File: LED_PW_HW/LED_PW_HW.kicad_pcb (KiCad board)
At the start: 2 copper layers, 44 x 44 mm, 0 parts

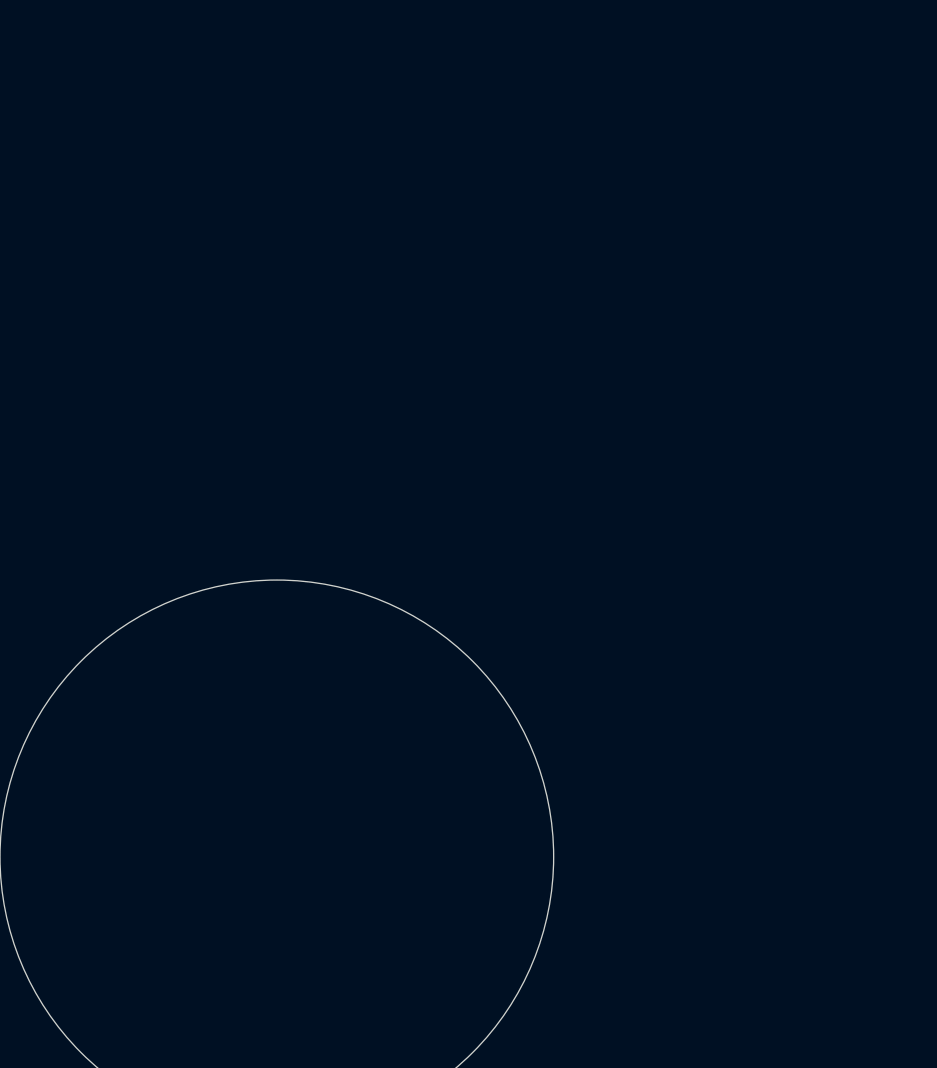
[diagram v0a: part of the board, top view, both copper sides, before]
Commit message: imported first footprints to pcb to get an idea
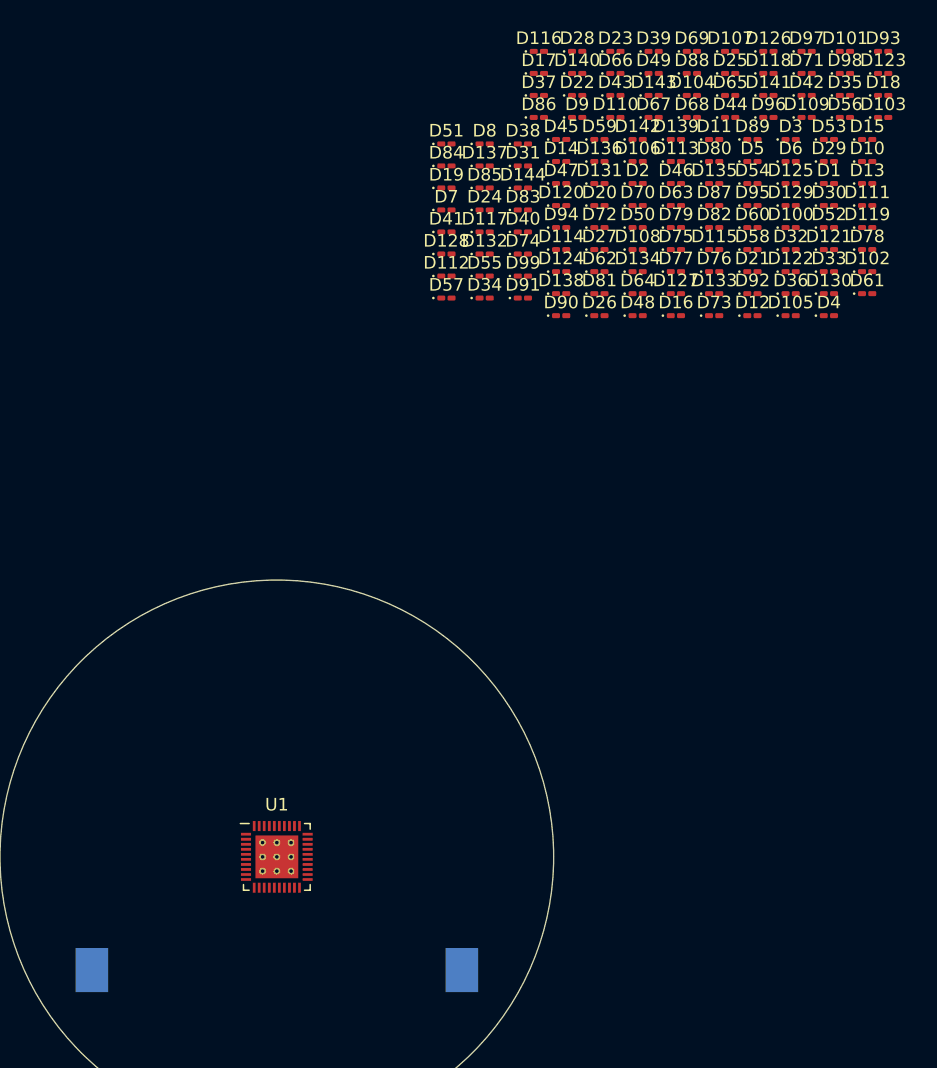
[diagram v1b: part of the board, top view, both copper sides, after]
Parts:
- added BT1: Battery_Holder, LED_PW_HW_Library:SMTU2032-LF, B.Cu at (140.0, 119.0)
- added D1: LED, LED_SMD:LED_0201_0603Metric_Pad0.64x0.40mm_HandSolder, F.Cu at (183.9, 56.5)
- added D10: LED, LED_SMD:LED_0201_0603Metric_Pad0.64x0.40mm_HandSolder, F.Cu at (186.9, 54.7)
- added D100: LED, LED_SMD:LED_0201_0603Metric_Pad0.64x0.40mm_HandSolder, F.Cu at (180.8, 60.0)
- added D101: LED, LED_SMD:LED_0201_0603Metric_Pad0.64x0.40mm_HandSolder, F.Cu at (185.1, 46.0)
- added D102: LED, LED_SMD:LED_0201_0603Metric_Pad0.64x0.40mm_HandSolder, F.Cu at (186.9, 63.5)
- added D103: LED, LED_SMD:LED_0201_0603Metric_Pad0.64x0.40mm_HandSolder, F.Cu at (188.2, 51.2)
- added D104: LED, LED_SMD:LED_0201_0603Metric_Pad0.64x0.40mm_HandSolder, F.Cu at (173.0, 49.5)
- added D105: LED, LED_SMD:LED_0201_0603Metric_Pad0.64x0.40mm_HandSolder, F.Cu at (180.8, 67.0)
- added D106: LED, LED_SMD:LED_0201_0603Metric_Pad0.64x0.40mm_HandSolder, F.Cu at (168.7, 54.7)
- added D107: LED, LED_SMD:LED_0201_0603Metric_Pad0.64x0.40mm_HandSolder, F.Cu at (176.0, 46.0)
- added D108: LED, LED_SMD:LED_0201_0603Metric_Pad0.64x0.40mm_HandSolder, F.Cu at (168.7, 61.7)
- added D109: LED, LED_SMD:LED_0201_0603Metric_Pad0.64x0.40mm_HandSolder, F.Cu at (182.1, 51.2)
- added D11: LED, LED_SMD:LED_0201_0603Metric_Pad0.64x0.40mm_HandSolder, F.Cu at (174.8, 53.0)
- added D110: LED, LED_SMD:LED_0201_0603Metric_Pad0.64x0.40mm_HandSolder, F.Cu at (166.9, 51.2)
- added D111: LED, LED_SMD:LED_0201_0603Metric_Pad0.64x0.40mm_HandSolder, F.Cu at (186.9, 58.2)
- added D112: LED, LED_SMD:LED_0201_0603Metric_Pad0.64x0.40mm_HandSolder, F.Cu at (153.5, 63.8)
- added D113: LED, LED_SMD:LED_0201_0603Metric_Pad0.64x0.40mm_HandSolder, F.Cu at (171.7, 54.7)
- added D114: LED, LED_SMD:LED_0201_0603Metric_Pad0.64x0.40mm_HandSolder, F.Cu at (162.6, 61.7)
- added D115: LED, LED_SMD:LED_0201_0603Metric_Pad0.64x0.40mm_HandSolder, F.Cu at (174.8, 61.7)
- added D116: LED, LED_SMD:LED_0201_0603Metric_Pad0.64x0.40mm_HandSolder, F.Cu at (160.8, 46.0)
- added D117: LED, LED_SMD:LED_0201_0603Metric_Pad0.64x0.40mm_HandSolder, F.Cu at (156.5, 60.3)
- added D118: LED, LED_SMD:LED_0201_0603Metric_Pad0.64x0.40mm_HandSolder, F.Cu at (179.1, 47.7)
- added D119: LED, LED_SMD:LED_0201_0603Metric_Pad0.64x0.40mm_HandSolder, F.Cu at (186.9, 60.0)
- added D12: LED, LED_SMD:LED_0201_0603Metric_Pad0.64x0.40mm_HandSolder, F.Cu at (177.8, 67.0)
- added D120: LED, LED_SMD:LED_0201_0603Metric_Pad0.64x0.40mm_HandSolder, F.Cu at (162.6, 58.2)
- added D121: LED, LED_SMD:LED_0201_0603Metric_Pad0.64x0.40mm_HandSolder, F.Cu at (183.9, 61.7)
- added D122: LED, LED_SMD:LED_0201_0603Metric_Pad0.64x0.40mm_HandSolder, F.Cu at (180.8, 63.5)
- added D123: LED, LED_SMD:LED_0201_0603Metric_Pad0.64x0.40mm_HandSolder, F.Cu at (188.2, 47.7)
- added D124: LED, LED_SMD:LED_0201_0603Metric_Pad0.64x0.40mm_HandSolder, F.Cu at (162.6, 63.5)
- added D125: LED, LED_SMD:LED_0201_0603Metric_Pad0.64x0.40mm_HandSolder, F.Cu at (180.8, 56.5)
- added D126: LED, LED_SMD:LED_0201_0603Metric_Pad0.64x0.40mm_HandSolder, F.Cu at (179.1, 46.0)
- added D127: LED, LED_SMD:LED_0201_0603Metric_Pad0.64x0.40mm_HandSolder, F.Cu at (171.7, 65.2)
- added D128: LED, LED_SMD:LED_0201_0603Metric_Pad0.64x0.40mm_HandSolder, F.Cu at (153.5, 62.1)
- added D129: LED, LED_SMD:LED_0201_0603Metric_Pad0.64x0.40mm_HandSolder, F.Cu at (180.8, 58.2)
- added D13: LED, LED_SMD:LED_0201_0603Metric_Pad0.64x0.40mm_HandSolder, F.Cu at (186.9, 56.5)
- added D130: LED, LED_SMD:LED_0201_0603Metric_Pad0.64x0.40mm_HandSolder, F.Cu at (183.9, 65.2)
- added D131: LED, LED_SMD:LED_0201_0603Metric_Pad0.64x0.40mm_HandSolder, F.Cu at (165.6, 56.5)
- added D132: LED, LED_SMD:LED_0201_0603Metric_Pad0.64x0.40mm_HandSolder, F.Cu at (156.5, 62.1)
- added D133: LED, LED_SMD:LED_0201_0603Metric_Pad0.64x0.40mm_HandSolder, F.Cu at (174.8, 65.2)
- added D134: LED, LED_SMD:LED_0201_0603Metric_Pad0.64x0.40mm_HandSolder, F.Cu at (168.7, 63.5)
- added D135: LED, LED_SMD:LED_0201_0603Metric_Pad0.64x0.40mm_HandSolder, F.Cu at (174.8, 56.5)
- added D136: LED, LED_SMD:LED_0201_0603Metric_Pad0.64x0.40mm_HandSolder, F.Cu at (165.6, 54.7)
- added D137: LED, LED_SMD:LED_0201_0603Metric_Pad0.64x0.40mm_HandSolder, F.Cu at (156.5, 55.1)
- added D138: LED, LED_SMD:LED_0201_0603Metric_Pad0.64x0.40mm_HandSolder, F.Cu at (162.6, 65.2)
- added D139: LED, LED_SMD:LED_0201_0603Metric_Pad0.64x0.40mm_HandSolder, F.Cu at (171.7, 53.0)
- added D14: LED, LED_SMD:LED_0201_0603Metric_Pad0.64x0.40mm_HandSolder, F.Cu at (162.6, 54.7)
- added D140: LED, LED_SMD:LED_0201_0603Metric_Pad0.64x0.40mm_HandSolder, F.Cu at (163.9, 47.7)
- added D141: LED, LED_SMD:LED_0201_0603Metric_Pad0.64x0.40mm_HandSolder, F.Cu at (179.1, 49.5)
- added D142: LED, LED_SMD:LED_0201_0603Metric_Pad0.64x0.40mm_HandSolder, F.Cu at (168.7, 53.0)
- added D143: LED, LED_SMD:LED_0201_0603Metric_Pad0.64x0.40mm_HandSolder, F.Cu at (169.9, 49.5)
- added D144: LED, LED_SMD:LED_0201_0603Metric_Pad0.64x0.40mm_HandSolder, F.Cu at (159.6, 56.8)
- added D15: LED, LED_SMD:LED_0201_0603Metric_Pad0.64x0.40mm_HandSolder, F.Cu at (186.9, 53.0)
- added D16: LED, LED_SMD:LED_0201_0603Metric_Pad0.64x0.40mm_HandSolder, F.Cu at (171.7, 67.0)
- added D17: LED, LED_SMD:LED_0201_0603Metric_Pad0.64x0.40mm_HandSolder, F.Cu at (160.8, 47.7)
- added D18: LED, LED_SMD:LED_0201_0603Metric_Pad0.64x0.40mm_HandSolder, F.Cu at (188.2, 49.5)
- added D19: LED, LED_SMD:LED_0201_0603Metric_Pad0.64x0.40mm_HandSolder, F.Cu at (153.5, 56.8)
- added D2: LED, LED_SMD:LED_0201_0603Metric_Pad0.64x0.40mm_HandSolder, F.Cu at (168.7, 56.5)
- added D20: LED, LED_SMD:LED_0201_0603Metric_Pad0.64x0.40mm_HandSolder, F.Cu at (165.6, 58.2)
- added D21: LED, LED_SMD:LED_0201_0603Metric_Pad0.64x0.40mm_HandSolder, F.Cu at (177.8, 63.5)
- added D22: LED, LED_SMD:LED_0201_0603Metric_Pad0.64x0.40mm_HandSolder, F.Cu at (163.9, 49.5)
- added D23: LED, LED_SMD:LED_0201_0603Metric_Pad0.64x0.40mm_HandSolder, F.Cu at (166.9, 46.0)
- added D24: LED, LED_SMD:LED_0201_0603Metric_Pad0.64x0.40mm_HandSolder, F.Cu at (156.5, 58.6)
- added D25: LED, LED_SMD:LED_0201_0603Metric_Pad0.64x0.40mm_HandSolder, F.Cu at (176.0, 47.7)
- added D26: LED, LED_SMD:LED_0201_0603Metric_Pad0.64x0.40mm_HandSolder, F.Cu at (165.6, 67.0)
- added D27: LED, LED_SMD:LED_0201_0603Metric_Pad0.64x0.40mm_HandSolder, F.Cu at (165.6, 61.7)
- added D28: LED, LED_SMD:LED_0201_0603Metric_Pad0.64x0.40mm_HandSolder, F.Cu at (163.9, 46.0)
- added D29: LED, LED_SMD:LED_0201_0603Metric_Pad0.64x0.40mm_HandSolder, F.Cu at (183.9, 54.7)
- added D3: LED, LED_SMD:LED_0201_0603Metric_Pad0.64x0.40mm_HandSolder, F.Cu at (180.8, 53.0)
- added D30: LED, LED_SMD:LED_0201_0603Metric_Pad0.64x0.40mm_HandSolder, F.Cu at (183.9, 58.2)
- added D31: LED, LED_SMD:LED_0201_0603Metric_Pad0.64x0.40mm_HandSolder, F.Cu at (159.6, 55.1)
- added D32: LED, LED_SMD:LED_0201_0603Metric_Pad0.64x0.40mm_HandSolder, F.Cu at (180.8, 61.7)
- added D33: LED, LED_SMD:LED_0201_0603Metric_Pad0.64x0.40mm_HandSolder, F.Cu at (183.9, 63.5)
- added D34: LED, LED_SMD:LED_0201_0603Metric_Pad0.64x0.40mm_HandSolder, F.Cu at (156.5, 65.6)
- added D35: LED, LED_SMD:LED_0201_0603Metric_Pad0.64x0.40mm_HandSolder, F.Cu at (185.1, 49.5)
- added D36: LED, LED_SMD:LED_0201_0603Metric_Pad0.64x0.40mm_HandSolder, F.Cu at (180.8, 65.2)
- added D37: LED, LED_SMD:LED_0201_0603Metric_Pad0.64x0.40mm_HandSolder, F.Cu at (160.8, 49.5)
- added D38: LED, LED_SMD:LED_0201_0603Metric_Pad0.64x0.40mm_HandSolder, F.Cu at (159.6, 53.3)
- added D39: LED, LED_SMD:LED_0201_0603Metric_Pad0.64x0.40mm_HandSolder, F.Cu at (169.9, 46.0)
- added D4: LED, LED_SMD:LED_0201_0603Metric_Pad0.64x0.40mm_HandSolder, F.Cu at (183.9, 67.0)
- added D40: LED, LED_SMD:LED_0201_0603Metric_Pad0.64x0.40mm_HandSolder, F.Cu at (159.6, 60.3)
- added D41: LED, LED_SMD:LED_0201_0603Metric_Pad0.64x0.40mm_HandSolder, F.Cu at (153.5, 60.3)
- added D42: LED, LED_SMD:LED_0201_0603Metric_Pad0.64x0.40mm_HandSolder, F.Cu at (182.1, 49.5)
- added D43: LED, LED_SMD:LED_0201_0603Metric_Pad0.64x0.40mm_HandSolder, F.Cu at (166.9, 49.5)
- added D44: LED, LED_SMD:LED_0201_0603Metric_Pad0.64x0.40mm_HandSolder, F.Cu at (176.0, 51.2)
- added D45: LED, LED_SMD:LED_0201_0603Metric_Pad0.64x0.40mm_HandSolder, F.Cu at (162.6, 53.0)
- added D46: LED, LED_SMD:LED_0201_0603Metric_Pad0.64x0.40mm_HandSolder, F.Cu at (171.7, 56.5)
- added D47: LED, LED_SMD:LED_0201_0603Metric_Pad0.64x0.40mm_HandSolder, F.Cu at (162.6, 56.5)
- added D48: LED, LED_SMD:LED_0201_0603Metric_Pad0.64x0.40mm_HandSolder, F.Cu at (168.7, 67.0)
- added D49: LED, LED_SMD:LED_0201_0603Metric_Pad0.64x0.40mm_HandSolder, F.Cu at (169.9, 47.7)
- added D5: LED, LED_SMD:LED_0201_0603Metric_Pad0.64x0.40mm_HandSolder, F.Cu at (177.8, 54.7)
- added D50: LED, LED_SMD:LED_0201_0603Metric_Pad0.64x0.40mm_HandSolder, F.Cu at (168.7, 60.0)
- added D51: LED, LED_SMD:LED_0201_0603Metric_Pad0.64x0.40mm_HandSolder, F.Cu at (153.5, 53.3)
- added D52: LED, LED_SMD:LED_0201_0603Metric_Pad0.64x0.40mm_HandSolder, F.Cu at (183.9, 60.0)
- added D53: LED, LED_SMD:LED_0201_0603Metric_Pad0.64x0.40mm_HandSolder, F.Cu at (183.9, 53.0)
- added D54: LED, LED_SMD:LED_0201_0603Metric_Pad0.64x0.40mm_HandSolder, F.Cu at (177.8, 56.5)
- added D55: LED, LED_SMD:LED_0201_0603Metric_Pad0.64x0.40mm_HandSolder, F.Cu at (156.5, 63.8)
- added D56: LED, LED_SMD:LED_0201_0603Metric_Pad0.64x0.40mm_HandSolder, F.Cu at (185.1, 51.2)
- added D57: LED, LED_SMD:LED_0201_0603Metric_Pad0.64x0.40mm_HandSolder, F.Cu at (153.5, 65.6)
- added D58: LED, LED_SMD:LED_0201_0603Metric_Pad0.64x0.40mm_HandSolder, F.Cu at (177.8, 61.7)
- added D59: LED, LED_SMD:LED_0201_0603Metric_Pad0.64x0.40mm_HandSolder, F.Cu at (165.6, 53.0)
- added D6: LED, LED_SMD:LED_0201_0603Metric_Pad0.64x0.40mm_HandSolder, F.Cu at (180.8, 54.7)
- added D60: LED, LED_SMD:LED_0201_0603Metric_Pad0.64x0.40mm_HandSolder, F.Cu at (177.8, 60.0)
- added D61: LED, LED_SMD:LED_0201_0603Metric_Pad0.64x0.40mm_HandSolder, F.Cu at (186.9, 65.2)
- added D62: LED, LED_SMD:LED_0201_0603Metric_Pad0.64x0.40mm_HandSolder, F.Cu at (165.6, 63.5)
- added D63: LED, LED_SMD:LED_0201_0603Metric_Pad0.64x0.40mm_HandSolder, F.Cu at (171.7, 58.2)
- added D64: LED, LED_SMD:LED_0201_0603Metric_Pad0.64x0.40mm_HandSolder, F.Cu at (168.7, 65.2)
- added D65: LED, LED_SMD:LED_0201_0603Metric_Pad0.64x0.40mm_HandSolder, F.Cu at (176.0, 49.5)
- added D66: LED, LED_SMD:LED_0201_0603Metric_Pad0.64x0.40mm_HandSolder, F.Cu at (166.9, 47.7)
- added D67: LED, LED_SMD:LED_0201_0603Metric_Pad0.64x0.40mm_HandSolder, F.Cu at (169.9, 51.2)
- added D68: LED, LED_SMD:LED_0201_0603Metric_Pad0.64x0.40mm_HandSolder, F.Cu at (173.0, 51.2)
- added D69: LED, LED_SMD:LED_0201_0603Metric_Pad0.64x0.40mm_HandSolder, F.Cu at (173.0, 46.0)
- added D7: LED, LED_SMD:LED_0201_0603Metric_Pad0.64x0.40mm_HandSolder, F.Cu at (153.5, 58.6)
- added D70: LED, LED_SMD:LED_0201_0603Metric_Pad0.64x0.40mm_HandSolder, F.Cu at (168.7, 58.2)
- added D71: LED, LED_SMD:LED_0201_0603Metric_Pad0.64x0.40mm_HandSolder, F.Cu at (182.1, 47.7)
- added D72: LED, LED_SMD:LED_0201_0603Metric_Pad0.64x0.40mm_HandSolder, F.Cu at (165.6, 60.0)
- added D73: LED, LED_SMD:LED_0201_0603Metric_Pad0.64x0.40mm_HandSolder, F.Cu at (174.8, 67.0)
- added D74: LED, LED_SMD:LED_0201_0603Metric_Pad0.64x0.40mm_HandSolder, F.Cu at (159.6, 62.1)
- added D75: LED, LED_SMD:LED_0201_0603Metric_Pad0.64x0.40mm_HandSolder, F.Cu at (171.7, 61.7)
- added D76: LED, LED_SMD:LED_0201_0603Metric_Pad0.64x0.40mm_HandSolder, F.Cu at (174.8, 63.5)
- added D77: LED, LED_SMD:LED_0201_0603Metric_Pad0.64x0.40mm_HandSolder, F.Cu at (171.7, 63.5)
- added D78: LED, LED_SMD:LED_0201_0603Metric_Pad0.64x0.40mm_HandSolder, F.Cu at (186.9, 61.7)
- added D79: LED, LED_SMD:LED_0201_0603Metric_Pad0.64x0.40mm_HandSolder, F.Cu at (171.7, 60.0)
- added D8: LED, LED_SMD:LED_0201_0603Metric_Pad0.64x0.40mm_HandSolder, F.Cu at (156.5, 53.3)
- added D80: LED, LED_SMD:LED_0201_0603Metric_Pad0.64x0.40mm_HandSolder, F.Cu at (174.8, 54.7)
- added D81: LED, LED_SMD:LED_0201_0603Metric_Pad0.64x0.40mm_HandSolder, F.Cu at (165.6, 65.2)
- added D82: LED, LED_SMD:LED_0201_0603Metric_Pad0.64x0.40mm_HandSolder, F.Cu at (174.8, 60.0)
- added D83: LED, LED_SMD:LED_0201_0603Metric_Pad0.64x0.40mm_HandSolder, F.Cu at (159.6, 58.6)
- added D84: LED, LED_SMD:LED_0201_0603Metric_Pad0.64x0.40mm_HandSolder, F.Cu at (153.5, 55.1)
- added D85: LED, LED_SMD:LED_0201_0603Metric_Pad0.64x0.40mm_HandSolder, F.Cu at (156.5, 56.8)
- added D86: LED, LED_SMD:LED_0201_0603Metric_Pad0.64x0.40mm_HandSolder, F.Cu at (160.8, 51.2)
- added D87: LED, LED_SMD:LED_0201_0603Metric_Pad0.64x0.40mm_HandSolder, F.Cu at (174.8, 58.2)
- added D88: LED, LED_SMD:LED_0201_0603Metric_Pad0.64x0.40mm_HandSolder, F.Cu at (173.0, 47.7)
- added D89: LED, LED_SMD:LED_0201_0603Metric_Pad0.64x0.40mm_HandSolder, F.Cu at (177.8, 53.0)
- added D9: LED, LED_SMD:LED_0201_0603Metric_Pad0.64x0.40mm_HandSolder, F.Cu at (163.9, 51.2)
- added D90: LED, LED_SMD:LED_0201_0603Metric_Pad0.64x0.40mm_HandSolder, F.Cu at (162.6, 67.0)
- added D91: LED, LED_SMD:LED_0201_0603Metric_Pad0.64x0.40mm_HandSolder, F.Cu at (159.6, 65.6)
- added D92: LED, LED_SMD:LED_0201_0603Metric_Pad0.64x0.40mm_HandSolder, F.Cu at (177.8, 65.2)
- added D93: LED, LED_SMD:LED_0201_0603Metric_Pad0.64x0.40mm_HandSolder, F.Cu at (188.2, 46.0)
- added D94: LED, LED_SMD:LED_0201_0603Metric_Pad0.64x0.40mm_HandSolder, F.Cu at (162.6, 60.0)
- added D95: LED, LED_SMD:LED_0201_0603Metric_Pad0.64x0.40mm_HandSolder, F.Cu at (177.8, 58.2)
- added D96: LED, LED_SMD:LED_0201_0603Metric_Pad0.64x0.40mm_HandSolder, F.Cu at (179.1, 51.2)
- added D97: LED, LED_SMD:LED_0201_0603Metric_Pad0.64x0.40mm_HandSolder, F.Cu at (182.1, 46.0)
- added D98: LED, LED_SMD:LED_0201_0603Metric_Pad0.64x0.40mm_HandSolder, F.Cu at (185.1, 47.7)
- added D99: LED, LED_SMD:LED_0201_0603Metric_Pad0.64x0.40mm_HandSolder, F.Cu at (159.6, 63.8)
- added U1: IS31FL3732A, LED_PW_HW_Library:IS31FL3732A, F.Cu at (140.0, 110.0)

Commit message: experimenting with plugin
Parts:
- moved D4 1023.4 mm to (329.0, 1080.1)
- moved D12 1015.5 mm to (329.0, 1071.2)
- moved D73 1007.1 mm to (329.0, 1062.2)
- moved D26 999.7 mm to (329.0, 1053.3)
- moved D105 988.5 mm to (329.0, 1044.4)
- moved D16 981.1 mm to (329.0, 1035.4)
- moved D48 972.8 mm to (329.0, 1026.5)
- moved D34 967.5 mm to (329.0, 1017.6)
- moved D57 959.2 mm to (329.0, 1008.6)
- moved D91 949.4 mm to (329.0, 999.7)
- moved D133 938.3 mm to (329.0, 990.8)
- moved D36 928.5 mm to (329.0, 981.8)
- moved D81 922.3 mm to (329.0, 972.9)
- moved D127 912.4 mm to (329.0, 964.0)
- moved D130 901.6 mm to (329.0, 955.1)
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
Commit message: sorting the leds
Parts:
- moved D12 1060.3 mm to (145.0, 27.0)
- moved D26 1034.5 mm to (164.0, 32.0)
- moved D73 1033.6 mm to (176.0, 40.0)
- moved D16 1029.4 mm to (143.0, 23.0)
- moved D4 1009.7 mm to (256.0, 73.0)
- moved D34 1004.0 mm to (192.0, 23.0)
- moved D48 1002.7 mm to (237.0, 28.0)
- moved D105 1000.1 mm to (271.0, 46.0)
- moved D57 980.4 mm to (271.0, 30.0)
- moved D36 966.9 mm to (197.0, 24.0)
- moved D91 963.1 mm to (237.0, 41.0)
- moved D81 940.3 mm to (204.0, 41.0)
- moved D133 926.1 mm to (205.0, 73.0)
- moved D61 922.3 mm to (142.0, 43.0)
- moved D127 909.2 mm to (158.0, 71.0)
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
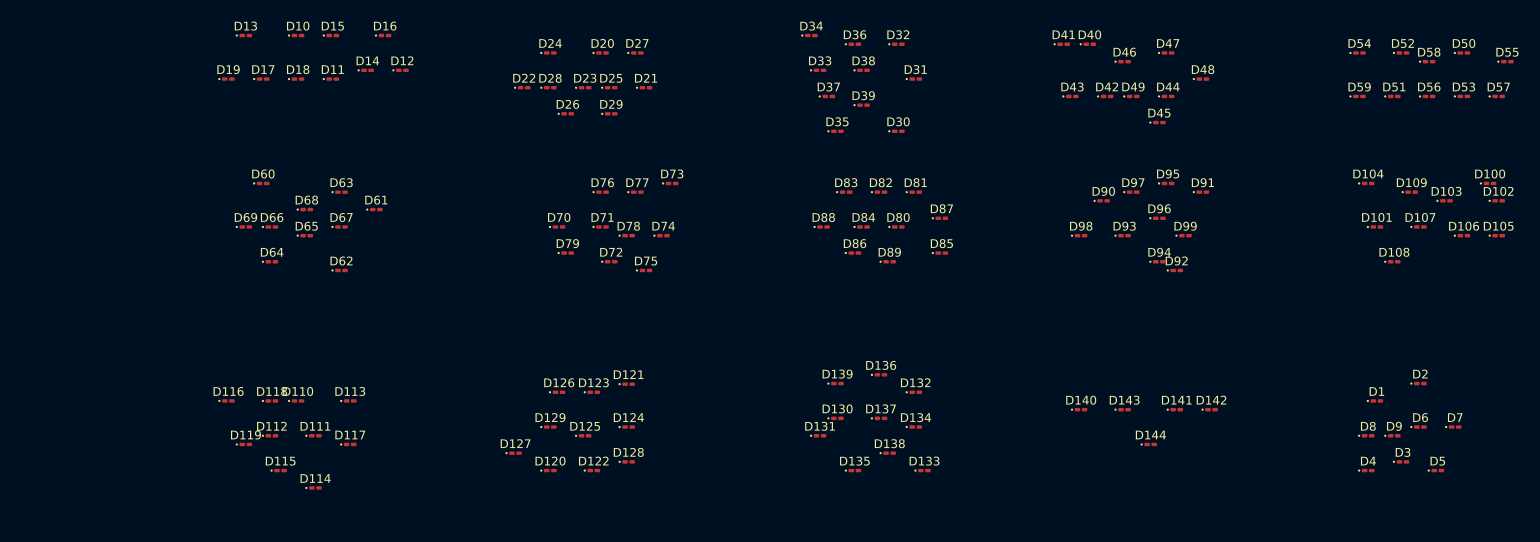
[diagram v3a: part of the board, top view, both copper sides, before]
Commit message: sorted leds
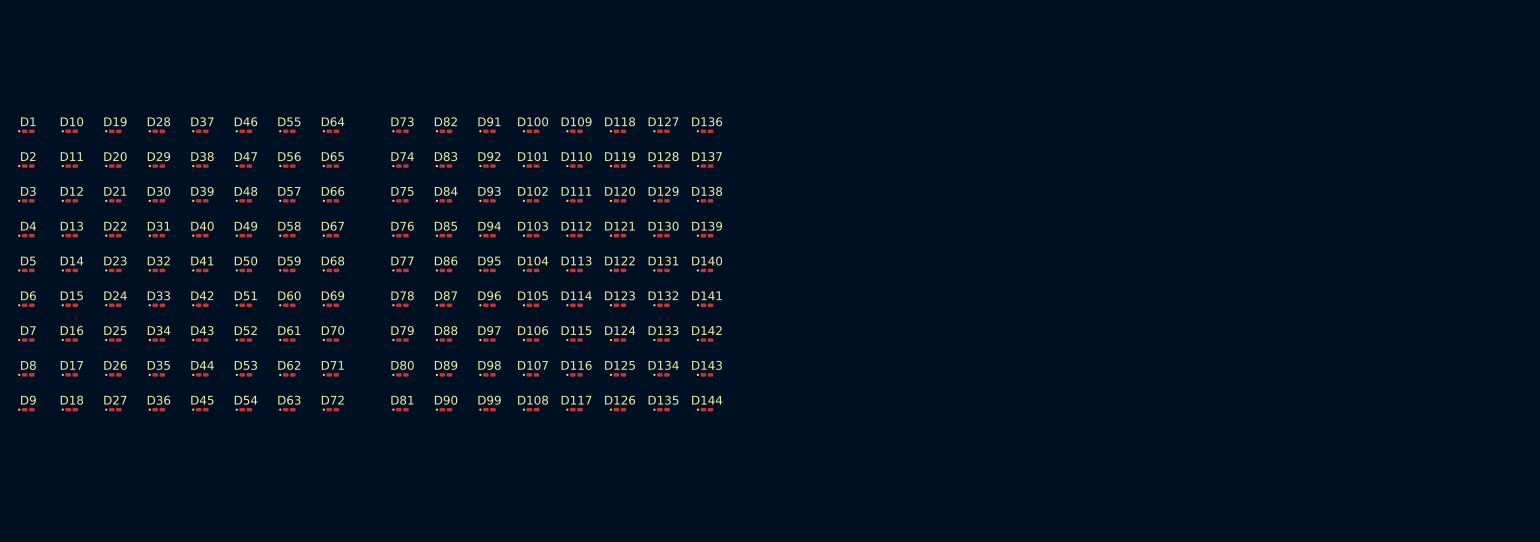
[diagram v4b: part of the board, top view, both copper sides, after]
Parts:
- moved D7 164.3 mm to (102.0, 58.0)
- moved D5 163.6 mm to (102.0, 50.0)
- moved D2 161.9 mm to (102.0, 38.0)
- moved D3 160.8 mm to (102.0, 42.0)
- moved D6 160.6 mm to (102.0, 54.0)
- moved D1 158.1 mm to (102.0, 34.0)
- moved D9 157.0 mm to (102.0, 66.0)
- moved D4 156.3 mm to (102.0, 46.0)
- moved D8 154.2 mm to (102.0, 62.0)
- moved D53 143.6 mm to (127.0, 62.0)
- moved D50 142.2 mm to (127.0, 50.0)
- moved D55 140.2 mm to (132.0, 34.0)
- moved D57 139.5 mm to (132.0, 42.0)
- moved D52 137.0 mm to (127.0, 58.0)
- moved D54 134.4 mm to (127.0, 66.0)
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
